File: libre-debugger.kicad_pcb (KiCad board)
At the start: 2 copper layers, 50 x 60 mm, 76 parts, among them J1 USB_C_Receptacle_USB2.0, J2 Conn_ST_STDC14, J4 Conn_01x10, Q1 2N7002, SW1 SW_SPDT, SW2 SW_Push, U1 FT2232H, U10 74LVC1G125, U11 74LVC1G125, U12 74LVC1G125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

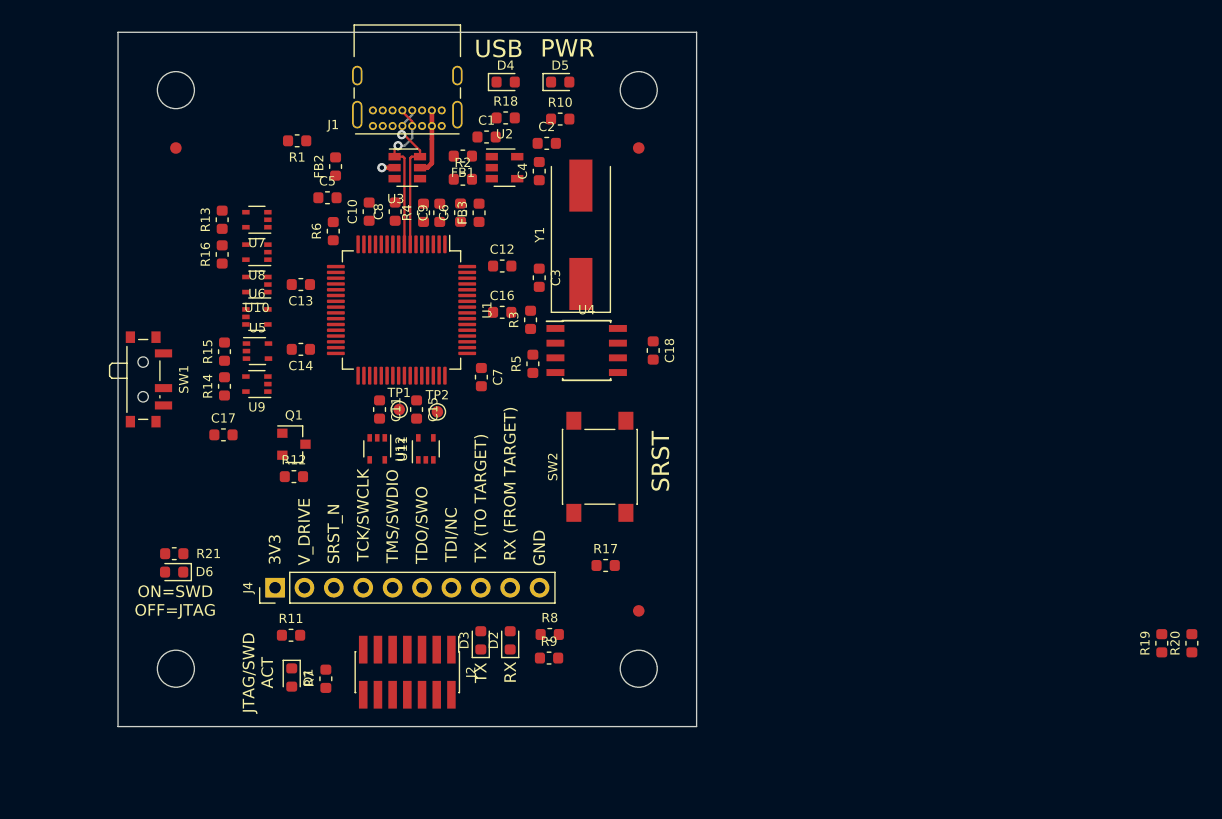
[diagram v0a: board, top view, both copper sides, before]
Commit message: Progress placement.
Most components placed.
Most routing pending.
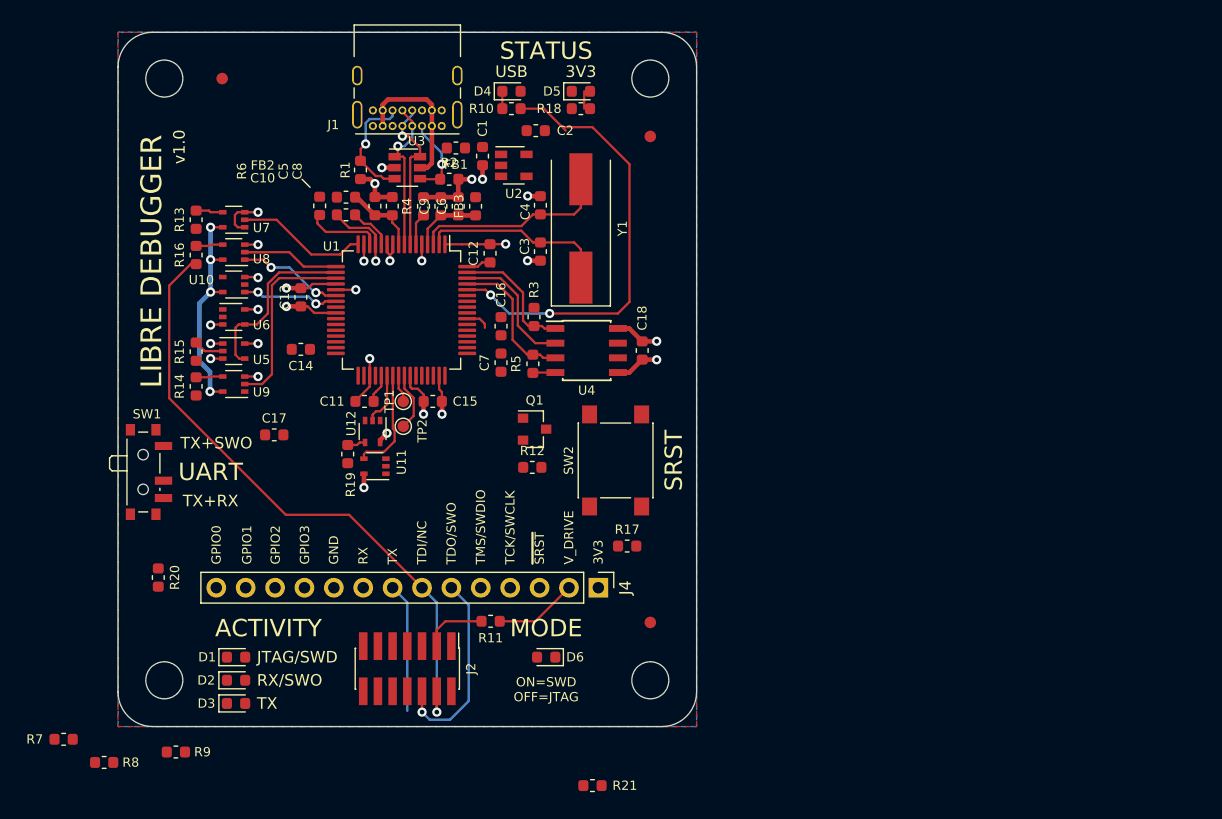
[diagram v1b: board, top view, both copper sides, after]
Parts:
- added LOGO1: Logo_Open_Hardware_Small, Symbol:OSHW-Logo_5.7x6mm_SilkScreen, B.Cu at (114.2, 55.0)
- J4: value Conn_01x10 -> Conn_01x14; footprint Connector_PinHeader_2.54mm:PinHeader_1x10_P2.54mm_Vertical -> Connector_PinHeader_2.54mm:PinHeader_1x14_P2.54mm_Vertical
- R10, R18, R21, R7, R8, R9: value 220R -> 470R
- R6: value 10k, 100k -> 10k
- moved R20 89.5 mm to (103.5, 97.1), turned to -90 degrees
- moved R19 72.2 mm to (119.8, 86.5)
- moved R21 41.3 mm to (141.0, 115.1)
- moved R8 40.1 mm to (98.8, 113.1), turned to 180 degrees
- moved R9 33.3 mm to (105.0, 112.2), turned to 180 degrees
- moved D6 33.0 mm to (137.0, 104.0)
- moved J4 27.9 mm to (141.5, 98.0), turned to -90 degrees
- moved D2 23.9 mm to (110.2, 106.0), turned to 0 degrees
- moved R7 23.3 mm to (95.3, 111.1), turned to 180 degrees
- moved D3 21.8 mm to (110.2, 108.0), turned to 0 degrees
- moved Q1 20.8 mm to (136.0, 84.3)
- moved R12 20.6 mm to (135.8, 87.6)
- moved R11 17.3 mm to (132.2, 100.9)
- moved SW1 8.00 mm to (102.5, 88.0)
- moved FID1 7.21 mm to (109.0, 54.0)
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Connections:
- U1 pad 26: Net-(U1-Pad26) -> /GPIO0
- U1 pad 27: Net-(U1-Pad27) -> /GPIO1
- U1 pad 28: Net-(U1-Pad28) -> /GPIO2
- U1 pad 29: Net-(U1-Pad29) -> /GPIO3
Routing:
- net GND: track 1.10 -> 56.8 mm, vias 1 -> 21
- net /TDI_TRGT: track 0.00 -> 41.5 mm
- net /USB_LED_N: track 0.00 -> 38.7 mm, vias 0 -> 2
- net Vdrive: track 0.00 -> 27.5 mm, vias 0 -> 5
- net /TCK_TRGT: track 0.00 -> 17.2 mm, vias 0 -> 1
- net /OSCO: track 0.00 -> 17.1 mm
- net /OSCI: track 0.00 -> 16.4 mm
- net /TMS: track 0.00 -> 16.2 mm
- net +3V3: track 0.00 -> 15.9 mm, vias 0 -> 6
- net /TDO: track 0.00 -> 15.4 mm
- net /TMS_TRGT: track 0.00 -> 13.1 mm, vias 0 -> 1
- net /EE_DATA: track 0.00 -> 12.3 mm
- net /EE_CLK: track 0.00 -> 11.5 mm
- net /TCK: track 0.00 -> 11.4 mm
- net /TXD_TRGT: track 0.00 -> 11.2 mm
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- added copper zone on B.Cu, net GND
- added copper zone on F.Cu, net GND
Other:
- outline, holes or cut-outs redrawn
- net class Default: clearance 0.2 -> 0.15
- net class Power: clearance 0.2 -> 0.15
- rule trace_clearance: 0.2 -> 0.15
- rule trace_min: 0.2 -> 0.15
- board text added: "ACTIVITY"
- board text added: "CHANNEL A/0 = JTAG/SWD + GPIOs CHANNEL B/1 = UART"
- board text added: "GPIO0"
- board text added: "GPIO1"
- board text added: "GPIO2"
- board text added: "GPIO3"
- board text added: "JTAG/SWD"
- board text added: "LIBRE DEBUGGER"
- board text added: "MODE"
- board text added: "QR code!!!!!!!!"
- board text added: "RX/SWO"
- board text added: "STATUS"
- board text added: "TX+RX"
- board text added: "TX+SWO"
- board text added: "UART"
- board text added: "github.com/diegoherranz/libre-debugger"
- board text added: "v1.0"
- board text added: "~SRST"
- board text removed: "JTAG/SWD ACT"
- board text removed: "PWR"
- board text removed: "SRST_N"

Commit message: PCB: reshuffle with new smaller crystal
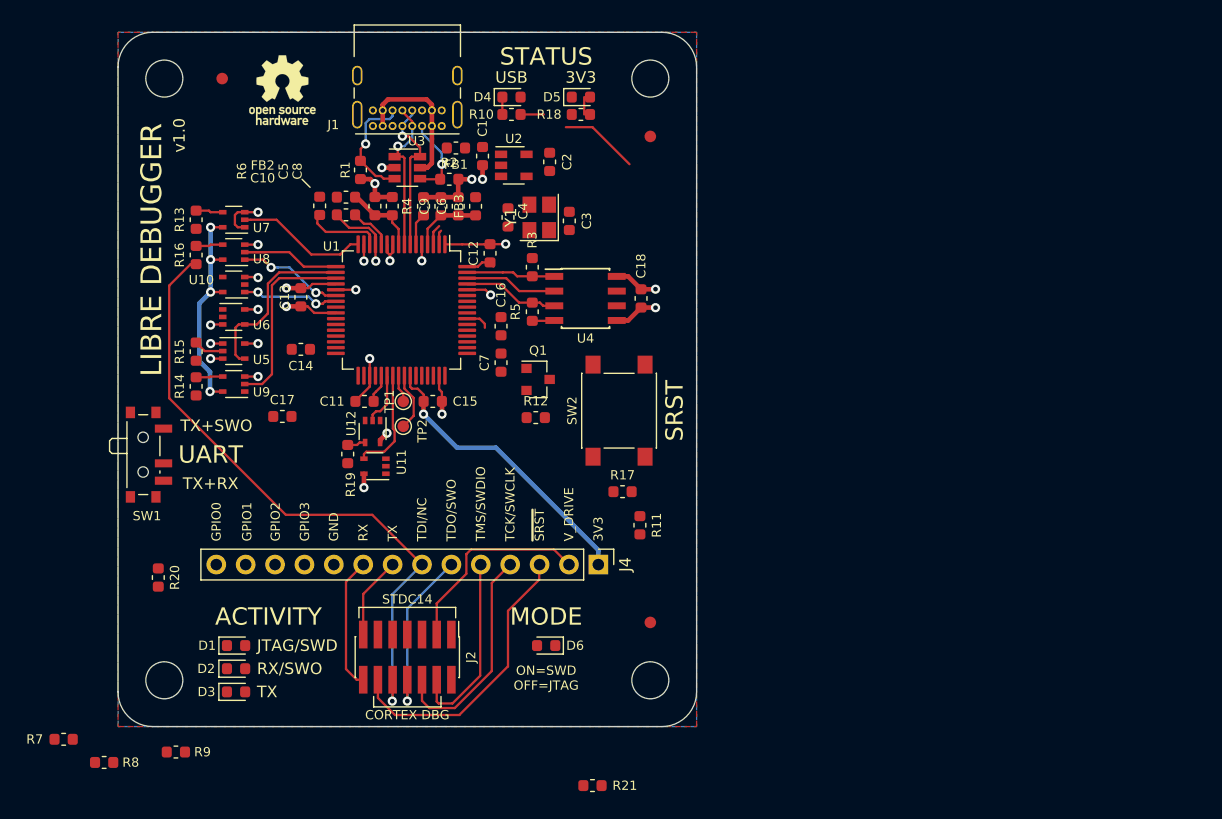
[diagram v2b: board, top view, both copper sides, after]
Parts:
- LOGO1: moved to F.Cu
- Y1: value 12 MHz -> Crystal_GND24; footprint Crystal:Crystal_SMD_HC49-SD -> Crystal:Crystal_SMD_3225-4Pin_3.2x2.5mm
- moved R11 15.3 mm to (145.1, 92.6), turned to 90 degrees
- moved R17 4.72 mm to (143.6, 89.7)
- moved C18 4.50 mm to (145.2, 73.0)
- moved U4 4.50 mm to (140.4, 73.0)
- moved R5 4.50 mm to (135.8, 74.2)
- moved Q1 4.31 mm to (136.3, 80.0)
- moved SW2 4.31 mm to (143.3, 82.7)
- moved R12 4.31 mm to (136.1, 83.3)
- moved R3 4.30 mm to (135.8, 70.3)
- moved Y1 3.72 mm to (136.4, 66.0)
- moved C3 3.64 mm to (139.0, 66.3), turned to 90 degrees
- moved C4 2.99 mm to (133.7, 66.0), turned to -90 degrees
- moved C2 2.95 mm to (137.3, 61.2), turned to -90 degrees
- moved J4 2.00 mm to (141.5, 96.0)
- moved C17 1.74 mm to (114.2, 83.2)
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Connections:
- J4 pad 2: Vdrive -> /VDRIVE_R
- Y1 pad 2: /OSCO -> GND
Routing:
- net /USB_LED_N: track 38.7 -> 11.0 mm, vias 2 -> 1
- net /SRST_N_TRGT: track 0.00 -> 25.1 mm
- net +3V3: track 15.9 -> 37.1 mm
- net /OSCO: track 17.1 -> 1.78 mm
- net /TDO_TRGT: track 0.00 -> 15.2 mm, vias 0 -> 1
- net /OSCI: track 16.4 -> 1.24 mm
- net /TDI_TRGT: track 41.5 -> 55.4 mm, vias 0 -> 1
- net /VDRIVE_R: track 5.58 -> 17.7 mm
- net /RXD_TRGT: track 0.00 -> 11.5 mm
- net Vdrive: track 27.5 -> 20.3 mm
- net /TXD_TRGT: track 11.2 -> 7.10 mm
- net /EE_DATA: track 12.3 -> 8.31 mm
- net /EE_CLK: track 11.5 -> 7.99 mm
- net /EE_CS: track 11.0 -> 7.67 mm
- net /TMS_TRGT: track 13.1 -> 16.3 mm, vias 1 -> 0
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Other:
- board text added: "CORTEX DBG"
- board text added: "STDC14"

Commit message: Lot of progress on the layout
Some notes:

- Top plane/fill is now 3V3
- Crystal fully routed
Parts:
- added C19: 100nF, Capacitor_SMD:C_0603_1608Metric, F.Cu at (110.0, 64.0)
- added C20: 100nF, Capacitor_SMD:C_0603_1608Metric, F.Cu at (106.8, 72.2)
- added C21: 100nF, Capacitor_SMD:C_0603_1608Metric, F.Cu at (110.0, 82.6)
- J4: value Conn_01x14 -> Conn_01x16; footprint Connector_PinHeader_2.54mm:PinHeader_1x14_P2.54mm_Vertical -> Connector_PinHeader_2.54mm:PinHeader_1x16_P2.54mm_Vertical
- moved J4 35.6 mm to (106.0, 96.0), turned to 90 degrees
- moved R11 35.4 mm to (109.7, 92.7)
- moved R17 16.8 mm to (127.0, 87.5), turned to 90 degrees
- moved R12 14.4 mm to (125.2, 92.7), turned to 90 degrees
- moved R7 14.1 mm to (104.0, 100.0)
- moved R21 13.2 mm to (137.0, 102.5), turned to 180 degrees
- moved R8 12.7 mm to (104.0, 101.5)
- moved C17 11.8 mm to (107.2, 92.7), turned to -90 degrees
- moved C3 6.79 mm to (132.4, 67.9), turned to -90 degrees
- moved R9 6.56 mm to (110.2, 108.2), turned to 0 degrees
- moved R3 3.59 mm to (139.3, 69.5), turned to 0 degrees
- moved Q1 2.71 mm to (136.6, 82.7)
- moved C4 1.70 mm to (132.4, 64.9), turned to 90 degrees
- moved Y1 1.66 mm to (134.9, 65.3)
- moved C14 1.50 mm to (117.0, 78.3), turned to -90 degrees
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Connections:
- net Net-(D6-Pad2) renamed /SWD_EN_LED
- J4 pad 10: GND -> /TXD_TRGT
- J4 pad 11: /GPIO3 -> /RXD_TRGT
- J4 pad 12: /GPIO2 -> /GPIO0
- J4 pad 14: /GPIO0 -> /GPIO2
- J4 pad 3: /SRST_N_TRGT -> GND
- J4 pad 5: /TMS_TRGT -> /TDI_TRGT
- J4 pad 7: /TDI_TRGT -> /TMS_TRGT
- J4 pad 8: /TXD_TRGT -> /SRST_N_TRGT
- J4 pad 9: /RXD_TRGT -> GND
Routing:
- net GND: track 54.6 -> 108.7 mm, vias 19 -> 36
- net /GPIO3: track 0.00 -> 41.4 mm
- net /GPIO2: track 0.00 -> 40.4 mm
- net /GPIO1: track 0.00 -> 40.1 mm
- net /GPIO0: track 0.00 -> 39.8 mm
- net /TCK_TRGT: track 19.3 -> 58.9 mm
- net /MPSSE_LED: track 0.00 -> 36.6 mm, vias 0 -> 2
- net Vdrive: track 20.3 -> 44.4 mm, vias 5 -> 6
- net /TDO_TRGT: track 15.2 -> 38.9 mm, vias 1 -> 0
- net /TMS_TRGT: track 16.3 -> 38.5 mm
- net +1V8: track 8.53 -> 30.1 mm, vias 0 -> 3
- net /SWD_EN: track 10.1 -> 30.4 mm, vias 3 -> 4
- net /SRST_N_TRGT: track 25.1 -> 5.10 mm, vias 0 -> 1
- net /SRST_N: track 1.72 -> 20.7 mm, vias 1 -> 0
- net /VDRIVE_R: track 17.7 -> 3.06 mm
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- added copper zone on F.Cu, net +3V3
- removed copper zone on F.Cu, net GND
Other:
- board text removed: "RX"

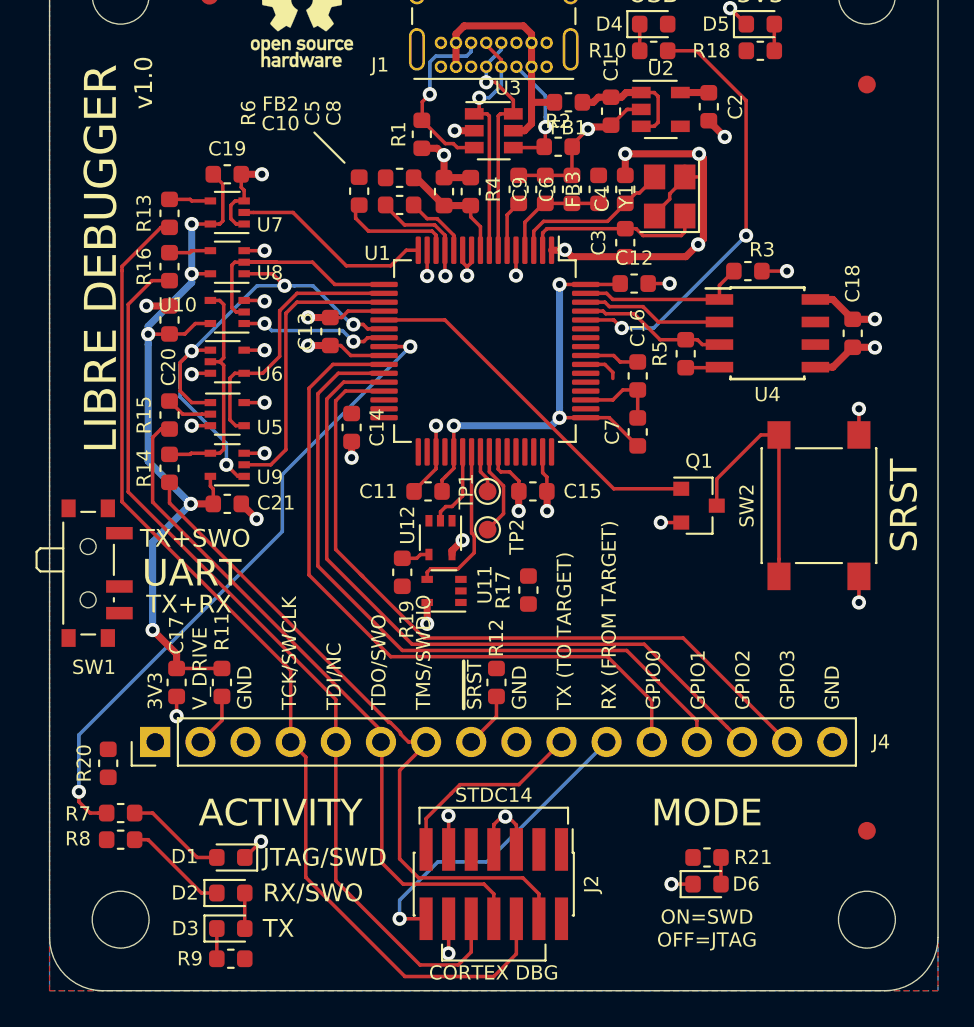
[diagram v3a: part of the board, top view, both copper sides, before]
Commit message: Layout routed completely. Needs clean-up and tidy-up.
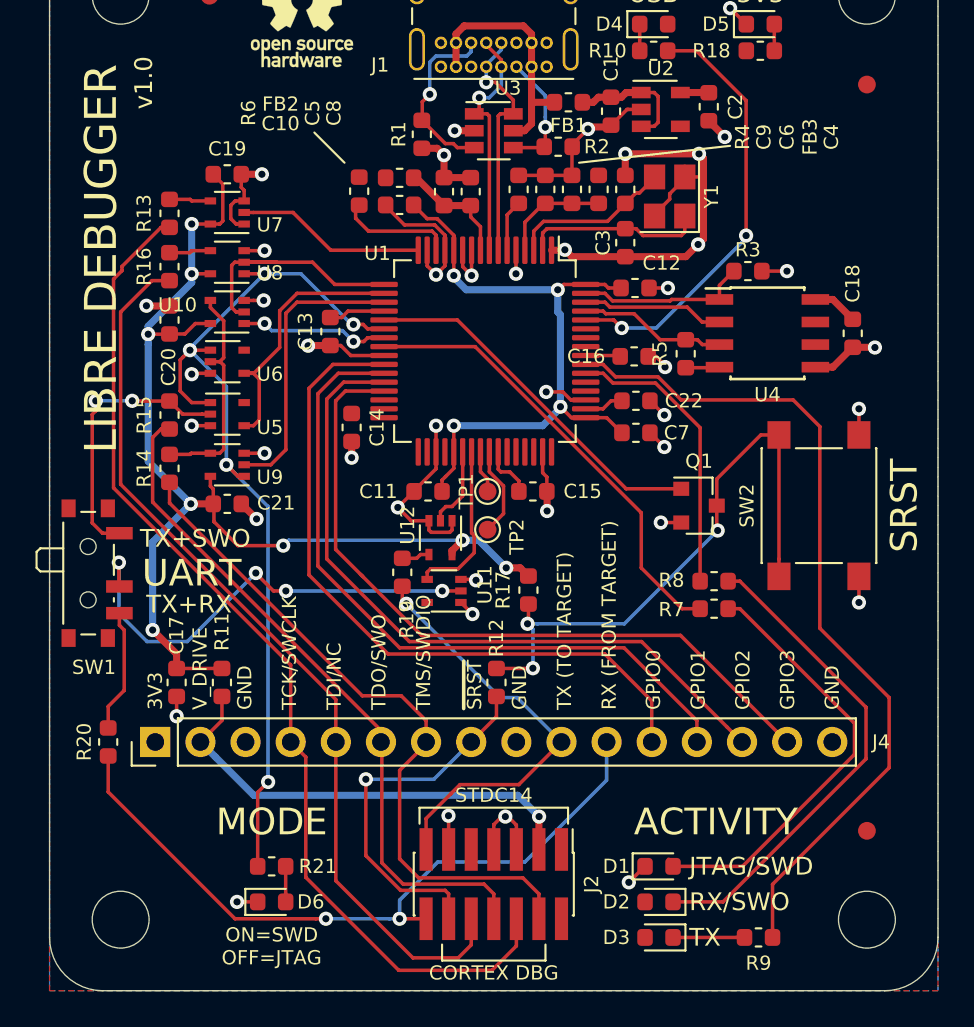
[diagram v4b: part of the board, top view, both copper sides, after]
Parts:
- added C22: 100nF, Capacitor_SMD:C_0603_1608Metric, F.Cu at (133.0, 76.8)
- moved R8 36.4 mm to (137.4, 87.0)
- moved R7 35.3 mm to (137.4, 88.5)
- moved R9 29.7 mm to (139.9, 107.0)
- moved D6 24.5 mm to (112.5, 105.0)
- moved R21 24.5 mm to (112.5, 103.0)
- moved D1 24.1 mm to (134.3, 103.0), turned to 0 degrees
- moved D2 24.1 mm to (134.3, 105.0), turned to 180 degrees
- moved D3 24.1 mm to (134.3, 107.0), turned to 180 degrees
- moved R20 1.20 mm to (103.3, 96.0)
- moved C16 1.12 mm to (132.9, 74.3), turned to 0 degrees
- moved C12 0.25 mm to (132.9, 70.5)
- moved C7 0.11 mm to (133.0, 78.6), turned to 0 degrees
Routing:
- net /TX_LED_N: track 2.05 -> 47.7 mm
- net /RXD_IN: track 0.00 -> 26.2 mm, vias 0 -> 4
- net /SWD_EN: track 30.4 -> 53.1 mm, vias 4 -> 5
- net /VDRIVE_R: track 3.06 -> 25.7 mm, vias 0 -> 1
- net /RXD_TRGT: track 17.9 -> 40.5 mm, vias 1 -> 2
- net /RX_LED_K: track 5.87 -> 27.8 mm
- net Vdrive: track 44.4 -> 64.7 mm, vias 6 -> 8
- net /SRST_N_R: track 14.0 -> 34.1 mm, vias 0 -> 3
- net /MPSSE_LED_A: track 5.66 -> 24.4 mm
- net /RX_LED_N: track 0.00 -> 16.3 mm
- net /SRST_N_TRGT: track 5.10 -> 21.2 mm
- net /TXD_TRGT: track 11.1 -> 24.2 mm, vias 0 -> 1
- net /TDO_R: track 2.61 -> 15.5 mm, vias 0 -> 2
- net /MPSSE_LED: track 36.6 -> 25.5 mm, vias 2 -> 0
- net GND: track 108.7 -> 117.9 mm, vias 36 -> 42
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
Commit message: Some layout tidy-up
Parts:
- moved R8 6.02 mm to (143.0, 89.2)
- moved R7 1.70 mm to (137.4, 86.8)
- moved U11 1.00 mm to (123.2, 87.5)
- moved R17 0.72 mm to (127.3, 86.8)
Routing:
- net /RX_LED_N: track 16.3 -> 25.5 mm
- net /RXD_IN: track 26.2 -> 21.8 mm
- net /RX_LED_K: track 27.8 -> 23.5 mm
- net /MPSSE_LED_A: track 24.4 -> 26.4 mm
- net /SRST_N_R: track 34.1 -> 36.0 mm, vias 3 -> 2
- net Vdrive: track 64.7 -> 62.8 mm
- net /MPSSE_LED: track 25.5 -> 24.5 mm
- net /RXD: track 9.24 -> 8.23 mm
- net /TX_LED_N: track 47.7 -> 48.2 mm
